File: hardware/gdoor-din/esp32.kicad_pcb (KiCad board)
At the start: 4 copper layers, 50 x 85 mm, 208 parts, among them J1 PlugIn_Terminal_Screw, J101 USB-C, J102 HR911105A, J103 EXP, J4 5V_IN, Q1 MMBT5401, Q2 MMBT2222A, SW101 RESET, SW102 BOOT, U1 TLV9351, U101 ESP32-S3-WROOM-1-N8R2, U102 USBLC6-2SC6, U103 AMS1117-3.3, U104 W5500, U2 LMV321, U3 LMV321, U5 ES8374, U6 LM393, U7 AMS1117-3.3, Y101 25MHz

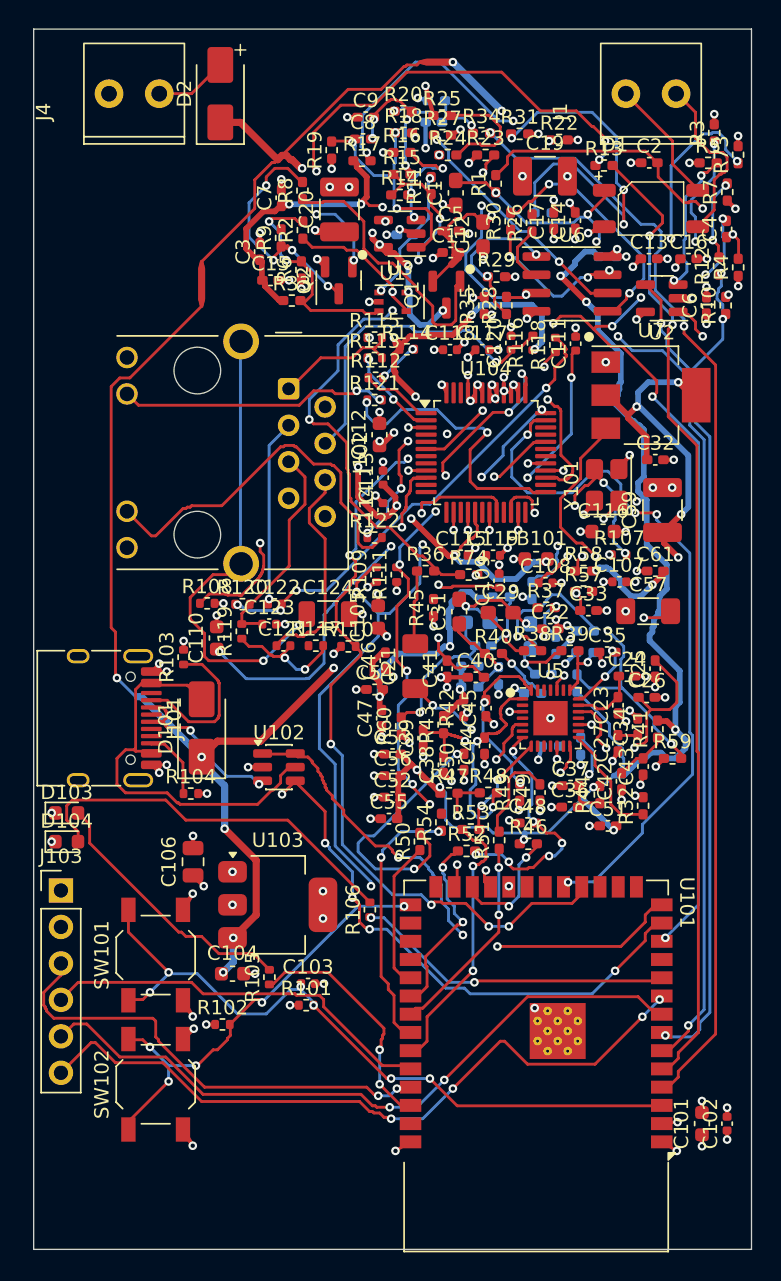
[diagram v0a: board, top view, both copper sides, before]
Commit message: DIN board: routing down to 5 open connections, DRC clean
Codec escape ring widened to 2.2 mm (15 passives moved), every U5 pin
has a straight escape stub, U5 GND pins tie inward to the exposed pad.
Remaining routing done with a scripted grid router (exact clearances,
rip-up); 5 connections around the W5500 crystal and the ES8374 are
still open, and several of those routes meander and need a clean-up.

esp32.kicad_dru: "PTH to Track" (0.33 mm) and "Pad to Track" (0.2 mm)
now apply to pads only. As written they also caught every via and
overrode the file's own 0.254 mm via rule (JLCPCB's via limit).

Co-Authored-By: Claude Opus 5.5 <noreply@anthropic.com>
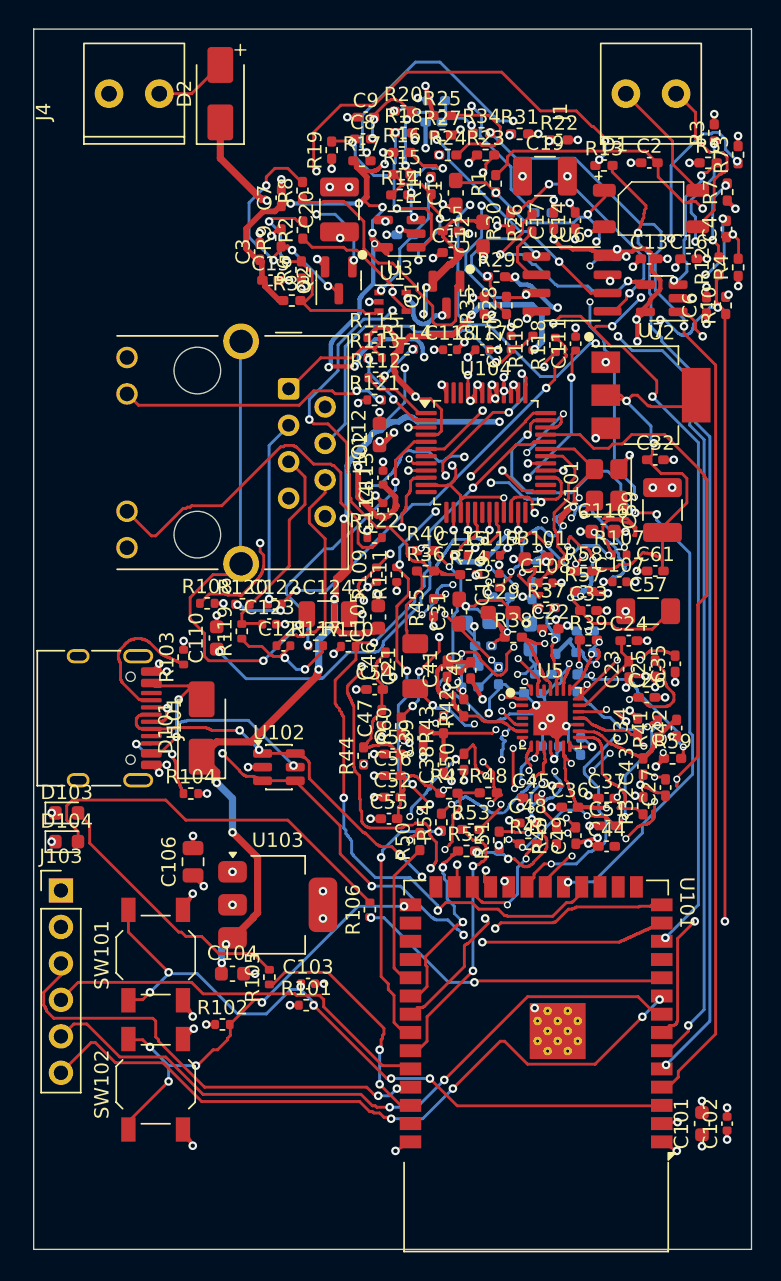
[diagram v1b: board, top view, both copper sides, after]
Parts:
- moved R44 16.7 mm to (123.0, 110.6)
- moved C44 11.0 mm to (139.9, 116.9), turned to 0 degrees
- moved R40 8.58 mm to (127.3, 96.3)
- moved C45 7.00 mm to (134.7, 113.5), turned to 0 degrees
- moved C42 5.34 mm to (144.8, 108.7)
- moved C35 4.80 mm to (144.7, 104.2), turned to 90 degrees
- moved C27 4.52 mm to (144.0, 112.8)
- moved R49 3.97 mm to (136.4, 116.2)
- moved C49 3.91 mm to (137.8, 116.2)
- moved C37 2.66 mm to (139.9, 113.6)
- moved C23 2.61 mm to (141.4, 104.6)
- moved C24 2.47 mm to (141.4, 102.6)
- moved R38 1.64 mm to (133.4, 102.4)
- moved R39 1.49 mm to (138.6, 102.6)
- moved C40 0.60 mm to (130.4, 104.7), turned to 90 degrees
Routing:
- net /MCU, USB, Power, Ethernet/ETH_SCK: track 0.00 -> 50.4 mm, vias 0 -> 4
- net /MCU, USB, Power, Ethernet/ETH_MISO: track 0.00 -> 48.9 mm, vias 0 -> 6
- net +3.3V: track 25.2 -> 58.0 mm, vias 35 -> 38
- net Net-(C28-Pad1): track 11.7 -> 41.2 mm, vias 1 -> 7
- net /MCU, USB, Power, Ethernet/+3.3V_ETHA: track 54.5 -> 82.7 mm, vias 13 -> 14
- net /MCU, USB, Power, Ethernet/ETH_XI: track 4.99 -> 29.9 mm, vias 3 -> 2
- net +3.3V_AUDIO: track 132.3 -> 107.5 mm, vias 13 -> 21
- net Net-(U5D-SPKVDD): track 3.00 -> 26.6 mm, vias 0 -> 4
- net Net-(U7-VI): track 23.6 -> 46.1 mm, vias 3 -> 9
- net Net-(U5A-MIC2P): track 4.15 -> 26.2 mm, vias 1 -> 2
- net GND: track 107.8 -> 129.6 mm, vias 140 -> 139
- net RX_ANA: track 65.6 -> 85.9 mm, vias 4 -> 6
- net +5V_onoff: track 37.6 -> 57.5 mm, vias 9 -> 12
- net /MCU, USB, Power, Ethernet/ETH_RXN_CHIP: track 0.00 -> 19.9 mm, vias 0 -> 2
- net Net-(U5B-CE): track 0.00 -> 17.5 mm, vias 0 -> 2
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
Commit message: gdoor-din: finish routing, 0.45/0.2 mm vias, drop unused mic options
- Route every net: kicad-cli DRC reports 0 unconnected, 0 errors,
  schematic parity clean.
- Project rules: min via 0.45 mm / drill 0.2 mm (JLCPCB standard on
  4 layers), Default netclass track 0.2 mm, via 0.45/0.2.
- Schematic: remove the option parts C28, C30, R61-R66, R67/R68 and
  their dangling wiring; keep R69-R72 (attenuation) and C62/C63
  (filtering). No-connects on the unused U5 speaker pins.

Open: one 0.07 mm +3.3V dangling stub, silk clean-up, F/B GND pours.

Co-Authored-By: Claude Opus 5.5 <noreply@anthropic.com>
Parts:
- removed C28, C30: 10u, Library:C_0603_1608Metric_Pad1.08x0.95mm_HandSolder
- removed R61, R62, R63, R64, R65, R66, R67, R68: 0, Library:R_0402_1005Metric_Pad0.72x0.64mm_HandSolder
- moved C103 27.3 mm to (145.5, 133.5), turned to 90 degrees
- moved C110 19.6 mm to (132.2, 100.4), turned to 0 degrees
- moved C61 16.7 mm to (134.5, 83.6)
- moved C33 13.9 mm to (137.8, 86.6), turned to 90 degrees
- moved C111 13.7 mm to (135.4, 95.4), turned to 0 degrees
- moved R40 13.2 mm to (140.2, 99.0), turned to 90 degrees
- moved C29 12.2 mm to (121.3, 105.4), turned to -90 degrees
- moved C109 10.7 mm to (137.4, 89.0)
- moved C57 9.60 mm to (146.9, 91.9), turned to 90 degrees
- moved C32 8.04 mm to (137.8, 84.1), turned to 90 degrees
- moved R69 6.60 mm to (128.6, 108.5)
- moved C107 6.25 mm to (137.4, 93.2), turned to -90 degrees
- moved R74 4.25 mm to (126.6, 100.1), turned to -90 degrees
- moved R72 4.10 mm to (136.4, 98.8)
- moved R70 3.60 mm to (141.5, 101.6)
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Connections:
- U5 pad 11: Net-(U5A-SPKN) -> unconnected-(U5A-SPKN-Pad11)
- U5 pad 14: Net-(U5A-SPKP) -> unconnected-(U5A-SPKP-Pad14)
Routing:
- net Net-(U5A-MICBIAS): track 15.5 -> 64.9 mm, vias 4 -> 9
- net unconnected-(U5A-SPKN-Pad11): track 0.00 -> 33.0 mm, vias 0 -> 4
- net Net-(U3--): track 45.4 -> 13.3 mm
- net /MCU, USB, Power, Ethernet/ETH_RXP_CHIP: track 11.9 -> 40.2 mm, vias 2 -> 5
- net +5V: track 154.3 -> 129.6 mm
- net Net-(U7-VI): track 46.1 -> 22.6 mm, vias 9 -> 2
- net Net-(C63-Pad1): track 41.2 -> 18.0 mm, vias 7 -> 3
- net +3.3V_AUDIO: track 107.5 -> 130.6 mm, vias 21 -> 25
- net /MCU, USB, Power, Ethernet/ETH_TOCAP: track 28.0 -> 7.11 mm
- net Net-(U5D-SPKVDD): track 26.6 -> 45.3 mm, vias 4 -> 3
- net +5V_onoff: track 57.5 -> 39.1 mm, vias 12 -> 8
- net Net-(R30-Pad1): track 51.5 -> 33.6 mm, vias 6 -> 7
- net Net-(D1-+): track 63.7 -> 46.9 mm
- net /MCU, USB, Power, Ethernet/ETH_XI: track 29.9 -> 13.1 mm, vias 2 -> 0
- net Net-(U5C-MCLK): track 29.2 -> 12.7 mm, vias 7 -> 4
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
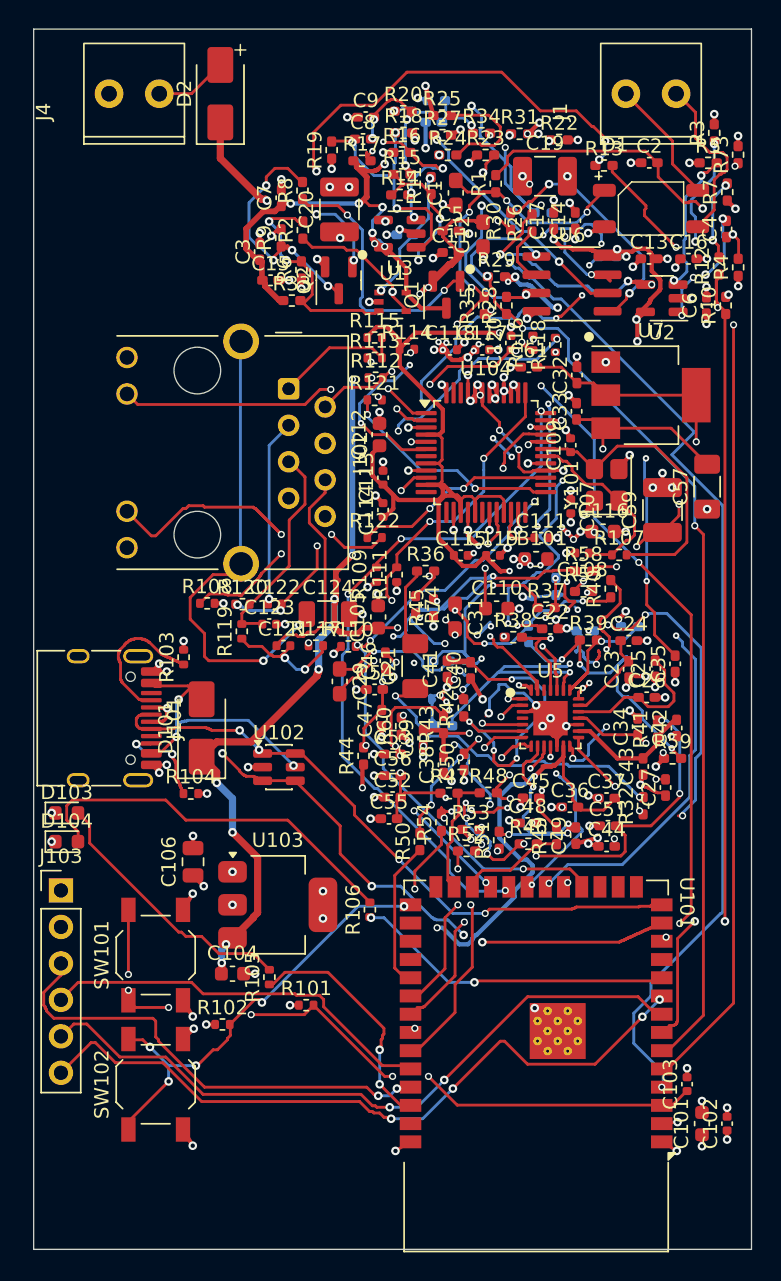
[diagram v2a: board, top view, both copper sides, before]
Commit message: gdoor-din: GND pours, stitching, antenna plane keepout, silk clean-up
- Remove the dangling +3.3V stub chain (7 items named by kicad-cli DRC).
- GND pours on F.Cu and B.Cu (0.2 mm clearance, thermal reliefs,
  islands removed) and 134 GND stitching vias at 0.45/0.2 on a 3 mm
  grid, placed only where they clear every other net.
- Rule area on In1/In2 under the ESP32-S3 antenna (the module's own
  keepout only covered F/B), so the inner planes no longer run under it.
- Reference text at 0.8 / 0.12 (Nobble convention), each placed clear of
  pads, silk and the edge; 158 visible, 39 in the densest 0402 clusters
  hidden (still on F.Fab). U101 antenna-end silk pulled inside the edge.
- DRU "Minimum Text" lowered from the JLC template's 1.0/0.15 to 0.8/0.12.

kicad-cli DRC: 0 errors, 0 unconnected, parity clean; silk_overlap,
silk_edge_clearance and silk_over_copper all 0. Only warning left:
lib_footprint_mismatch on U101.

Co-Authored-By: Claude Opus 5.5 <noreply@anthropic.com>
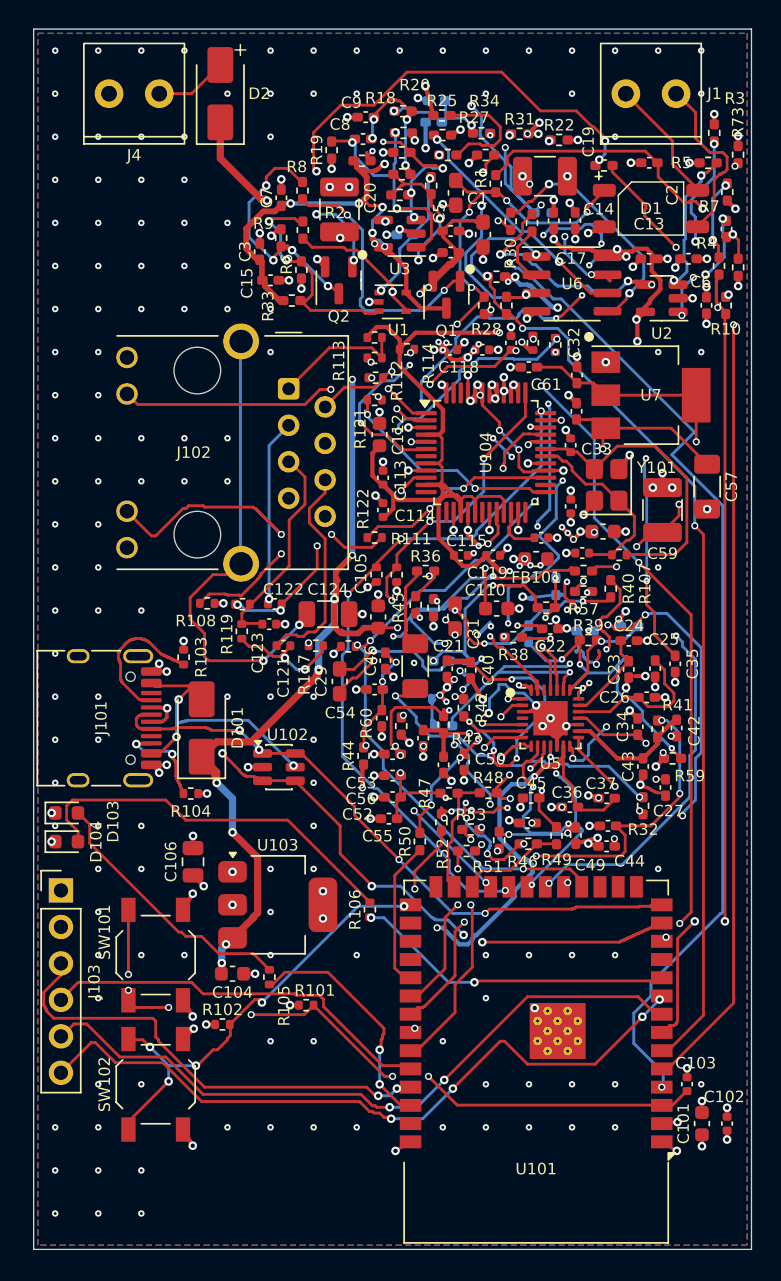
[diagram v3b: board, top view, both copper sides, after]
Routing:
- net +3.3V: track 72.3 -> 71.7 mm
- net GND: vias 147 -> 281
- added copper zone on B.Cu, net GND
- added copper zone on F.Cu, net GND

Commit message: gdoor-din: 1210 part for the 100u caps, unify resistor values for JLC BOM
JLCPCB flagged two BOM problems:
- C19, C20, C59 sit on 1210 pads but carried C15008, a 1206 6.3 V part
  (CL31A107MQHNNNE; same mismatch upstream). Now C23742
  (CL32A107MPVNNNE, 100 uF 10 V X5R 1210), which also gives C20 on +5V
  a sensible voltage margin.
- One part matched several BOM lines because the copied sheet spelled
  values "5k1"/"4k7" and the new sheet "5.1k"/"4.7k". R5, R7, R16, R17
  are now 5.1k and R26 4.7k.

The copied sheet's symbols carry stale Reference properties from the
upstream sheet, so Konnect edited the wrong symbols; the edit was keyed
on each symbol's live instance instead and the file rewritten by
kicad-cli sch upgrade. Netlist diff: exactly these 8 fields.
DRC: 0 errors, 0 unconnected, parity clean.

Co-Authored-By: Claude Opus 5.5 <noreply@anthropic.com>
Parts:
- R16, R17, R5, R7: value 5k1 -> 5.1k
- R26: value 4k7 -> 4.7k
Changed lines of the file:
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@@
 			)
 		)
-		(property "Value" "5k1"
+		(property "Value" "5.1k"
 			(at 0 1.17 0)
 			(layer "F.Fab")
@@
 			)
 		)
-		(property "Value" "5k1"
+		(property "Value" "5.1k"
 			(at 0 1.17 0)
 			(layer "F.Fab")
@@
 			)
 		)
-		(property "MPN" "C15008"
+		(property "MPN" "C23742"
 			(at 0 0 90)
 			(unlocked yes)
@@
 			)
 		)
-		(property "Value" "5k1"
+		(property "Value" "5.1k"
 			(at 0 1.17 90)
 			(layer "F.Fab")
@@
 			)
 		)
-		(property "Value" "4k7"
+		(property "Value" "4.7k"
 			(at 0 1.17 90)
 			(layer "F.Fab")
@@
 			)
 		)
-		(property "Value" "5k1"
+		(property "Value" "5.1k"
 			(at 0 1.17 0)
 			(layer "F.Fab")
@@
 			)
 		)
-		(property "MPN" "C15008"
+		(property "MPN" "C23742"
 			(at 0 0 90)
 			(unlocked yes)
@@
 			)
 		)
-		(property "MPN" "C15008"
+		(property "MPN" "C23742"
 			(at 0 0 0)
 			(unlocked yes)
